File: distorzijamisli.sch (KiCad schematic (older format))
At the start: 80 parts, among them J1 SW DBG, J12 5V, J2 USB_OTG, J3 Conn_02x16_Odd_Even, J4 Conn_02x16_Odd_Even, J5 Conn_02x08_Odd_Even, J6 Conn_02x03_Odd_Even, J7 Conn_02x03_Odd_Even, SW1 SW_Push, U1 STM32F407VGTx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

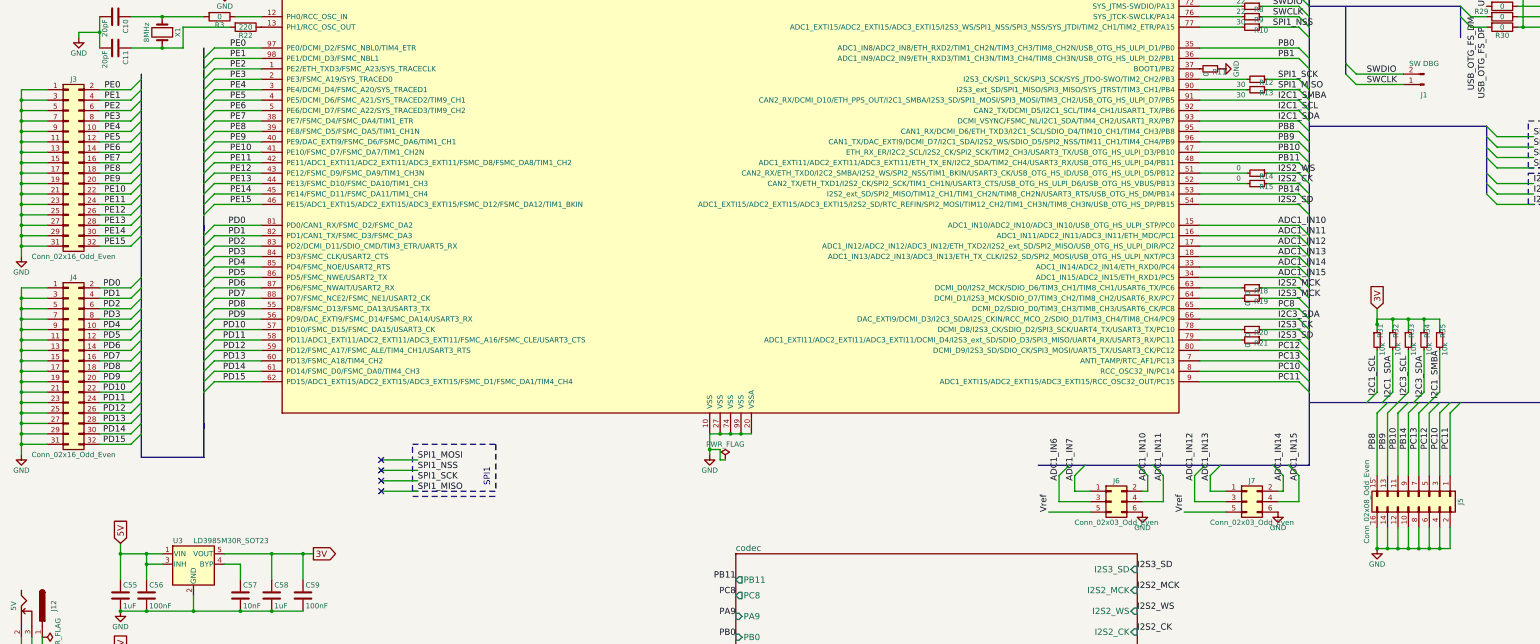
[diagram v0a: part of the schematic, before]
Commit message: Remove several port connectors from the board
As they take too much space, with the sparse pin
layout, we'll just remove them, as they have no use in this
application.
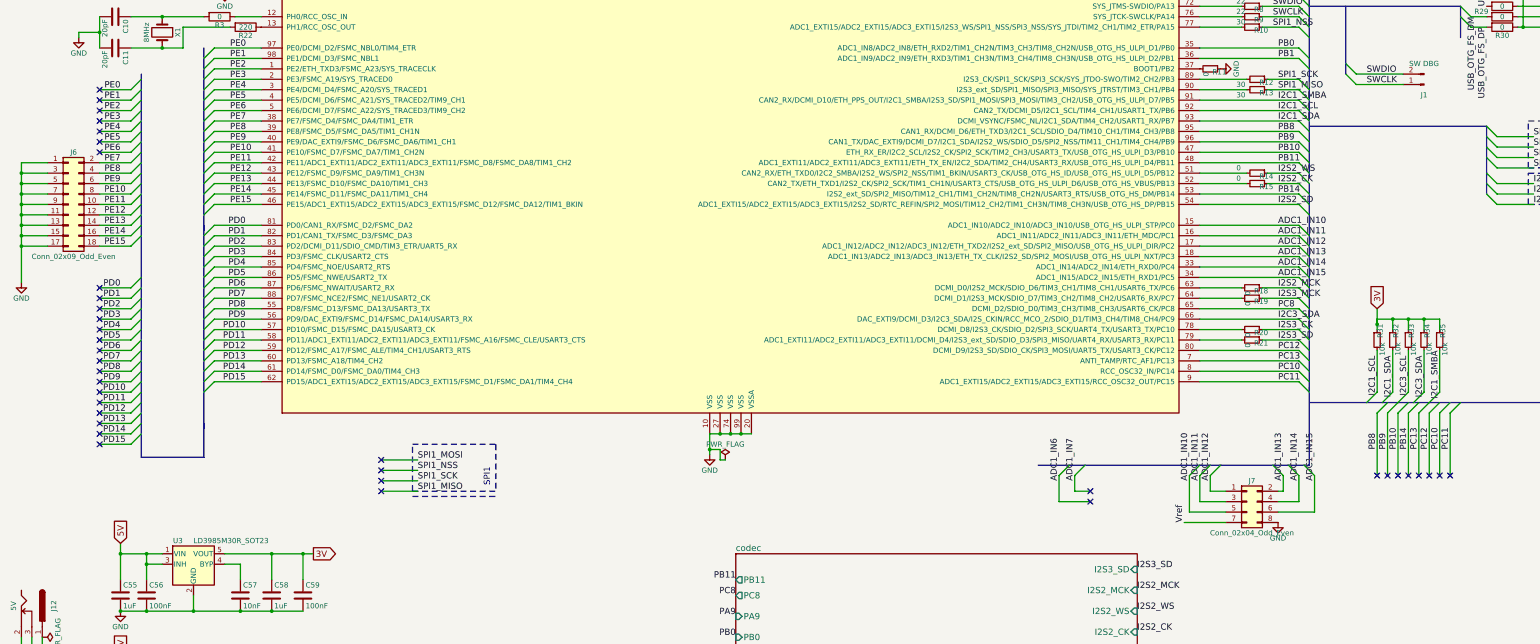
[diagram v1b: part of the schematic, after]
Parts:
- removed J3, J4: Conn_02x16_Odd_Even, Pin_Headers:Pin_Header_Straight_2x16, symbol Conn_02x16_Odd_Even
- removed J5: Conn_02x08_Odd_Even, Pin_Headers:Pin_Header_Straight_2x08, symbol Conn_02x08_Odd_Even
- removed J6, J7: Conn_02x03_Odd_Even, Pin_Headers:Pin_Header_Straight_2x03, symbol Conn_02x03_Odd_Even
- added J6: Conn_02x09_Odd_Even, Pin_Headers:Pin_Header_Straight_2x09, symbol Conn_02x09_Odd_Even
- added J7: Conn_02x04_Odd_Even, Pin_Headers:Pin_Header_Straight_2x04, symbol Conn_02x04_Odd_Even
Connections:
- net ADC1_IN10: now also J7.5 (Pin_5)
- net ADC1_IN11: now also J7.3 (Pin_3)
- net ADC1_IN12: now also J7.1 (Pin_1)
- net ADC1_IN13: now also J7.2 (Pin_2)
- net ADC1_IN14: now also J7.4 (Pin_4)
- net ADC1_IN15: now also J7.6 (Pin_6)
- net GND: now also J6.1 (Pin_1), J6.11 (Pin_11), J6.13 (Pin_13), J6.15 (Pin_15), J6.17 (Pin_17), J6.3 (Pin_3), J6.5 (Pin_5), J6.7 (Pin_7), J6.9 (Pin_9), J7.8 (Pin_8)
- net PE10: now also J6.8 (Pin_8)
- net PE11: now also J6.10 (Pin_10)
- net PE12: now also J6.12 (Pin_12)
- net PE13: now also J6.14 (Pin_14)
- net PE14: now also J6.16 (Pin_16)
- net PE15: now also J6.18 (Pin_18)
- net PE7: now also J6.2 (Pin_2)
- net PE8: now also J6.4 (Pin_4)
- net PE9: now also J6.6 (Pin_6)
- net Vref: now also J7.7 (Pin_7)
- no-connect marks 5 -> 38
